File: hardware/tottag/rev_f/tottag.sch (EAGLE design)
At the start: 154 parts, among them J1 MICRO_USB_B_HIROSE_ZX62-B-5PA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, J2 CON_MICRO_SDDM3AT-SF-PEJM5, J3 BAT_HOLE, J4 TC2030-JLINK-NL, J5 TC2030-JLINK-NL, T1 HHM1595A1, U1 DW1000, U10 STM32F091CC, U11 AB1815-T3, U2 FT232RQ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

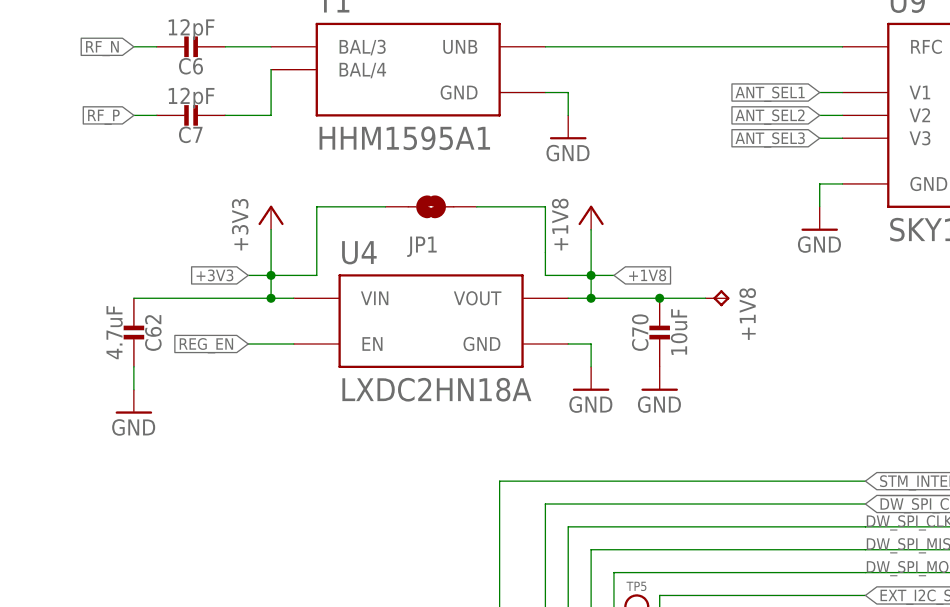
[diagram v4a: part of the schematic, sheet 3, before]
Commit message: Replace obsolete power regulator
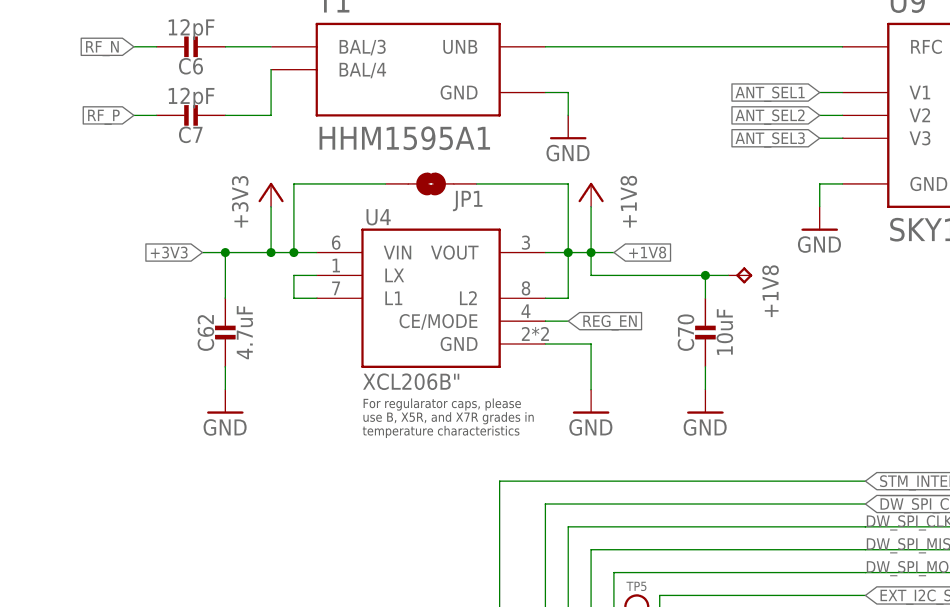
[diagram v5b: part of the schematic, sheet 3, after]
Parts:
- C70: device passives:CAPACITOR0603_CAP -> passives:CAPACITOR0402_CAP
- U4: value LXDC2HN18A -> XCL206B"; device regulators:LXDC2HN18A -> regulators:XCL206B"
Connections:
- new net N$44: U4.L1, U4.LX
- net +1V8: now also U4.L2
- net +3V3: now also C62.1; no longer C62.2
- net GND: now also C62.2; no longer C62.1
- net REG_EN: now also U4.CE/MODE; no longer U4.EN
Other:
- note added: "For regularator caps, please use B, X5R, and X7R grades in temperature characteristics"
- moved on the sheet: +1V8, C62, C70, JP1

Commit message: rev f cleanups
 - Fix footprint error in new regulator
 - Better shielding between 1.8V and debug signals
 - Better routing for `REG_EN` line
 - Clean up ground plane odditites
 - Remove vias from under RTC battery
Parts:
- U4: value XCL206B" -> (none); device regulators:XCL206B" -> regulators:XCL206B
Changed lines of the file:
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@@
 <attribute name="MPN" value="RC0402JR-0710KL"/>
 </part>
-<part name="U4" library="regulators" deviceset="XCL206B" device="&quot;"/>
 <part name="C62" library="passives" deviceset="CAPACITOR" device="0402_CAP" value="4.7uF"/>
 <part name="C70" library="passives" deviceset="CAPACITOR" device="0402_CAP" value="10uF"/>
+<part name="U4" library="regulators" deviceset="XCL206" device="B"/>
 </parts>
 <sheets>
@@
 <attribute name="VALUE" x="43.18" y="162.56" size="1.778" layer="96" font="vector" align="top-left" display="off"/>
 </instance>
-<instance part="U4" gate="G$1" x="45.72" y="152.4" smashed="yes">
-<attribute name="NAME" x="38.354" y="160.528" size="1.778" layer="95"/>
-<attribute name="VALUE" x="38.1" y="142.24" size="1.778" layer="96"/>
-</instance>
 <instance part="C62" gate="G$1" x="22.86" y="149.86" smashed="yes">
 <attribute name="NAME" x="21.59" y="148.59" size="1.778" layer="95" ratio="12" rot="R90" align="bottom-center"/>
@@
 <attribute name="VALUE" x="77.47" y="148.59" size="1.778" layer="96" ratio="12" rot="R270" align="bottom-center"/>
 </instance>
+<instance part="U4" gate="G$1" x="45.72" y="152.4" smashed="yes">
+<attribute name="NAME" x="38.354" y="160.528" size="1.778" layer="95"/>
+<attribute name="VALUE" x="38.1" y="142.24" size="1.778" layer="96"/>
+</instance>
 </instances>
 <busses>
@@
 <wire x1="60.96" y1="157.48" x2="63.5" y2="157.48" width="0.1524" layer="91"/>
 <pinref part="JP1" gate="G$1" pin="2"/>
-<pinref part="U4" gate="G$1" pin="VOUT"/>
 <wire x1="60.96" y1="157.48" x2="58.42" y2="157.48" width="0.1524" layer="91"/>
 <junction x="60.96" y="157.48"/>
 <wire x1="60.96" y1="157.48" x2="60.96" y2="152.4" width="0.1524" layer="91"/>
-<pinref part="U4" gate="G$1" pin="L2"/>
 <wire x1="60.96" y1="152.4" x2="58.42" y2="152.4" width="0.1524" layer="91"/>
 <pinref part="C70" gate="G$1" pin="1"/>
 <wire x1="76.2" y1="152.4" x2="76.2" y2="154.94" width="0.1524" layer="91"/>
 <junction x="76.2" y="154.94"/>
+<pinref part="U4" gate="G$1" pin="L2"/>
+<pinref part="U4" gate="G$1" pin="VOUT"/>
 </segment>
 <segment>
@@
 <wire x1="30.48" y1="165.1" x2="40.64" y2="165.1" width="0.1524" layer="91"/>
 <pinref part="JP1" gate="G$1" pin="1"/>
-<pinref part="U4" gate="G$1" pin="VIN"/>
 <wire x1="30.48" y1="157.48" x2="33.02" y2="157.48" width="0.1524" layer="91"/>
 <junction x="30.48" y="157.48"/>
@@
 <wire x1="22.86" y1="152.4" x2="22.86" y2="157.48" width="0.1524" layer="91"/>
 <junction x="22.86" y="157.48"/>
+<pinref part="U4" gate="G$1" pin="VIN"/>
 </segment>
 <segment>
@@
 <net name="N$44" class="0">
 <segment>
-<pinref part="U4" gate="G$1" pin="LX"/>
 <wire x1="33.02" y1="154.94" x2="30.48" y2="154.94" width="0.1524" layer="91"/>
 <wire x1="30.48" y1="154.94" x2="30.48" y2="152.4" width="0.1524" layer="91"/>
-<pinref part="U4" gate="G$1" pin="L1"/>
 <wire x1="30.48" y1="152.4" x2="33.02" y2="152.4" width="0.1524" layer="91"/>
+<pinref part="U4" gate="G$1" pin="LX"/>
+<pinref part="U4" gate="G$1" pin="L1"/>
 </segment>
 </net>

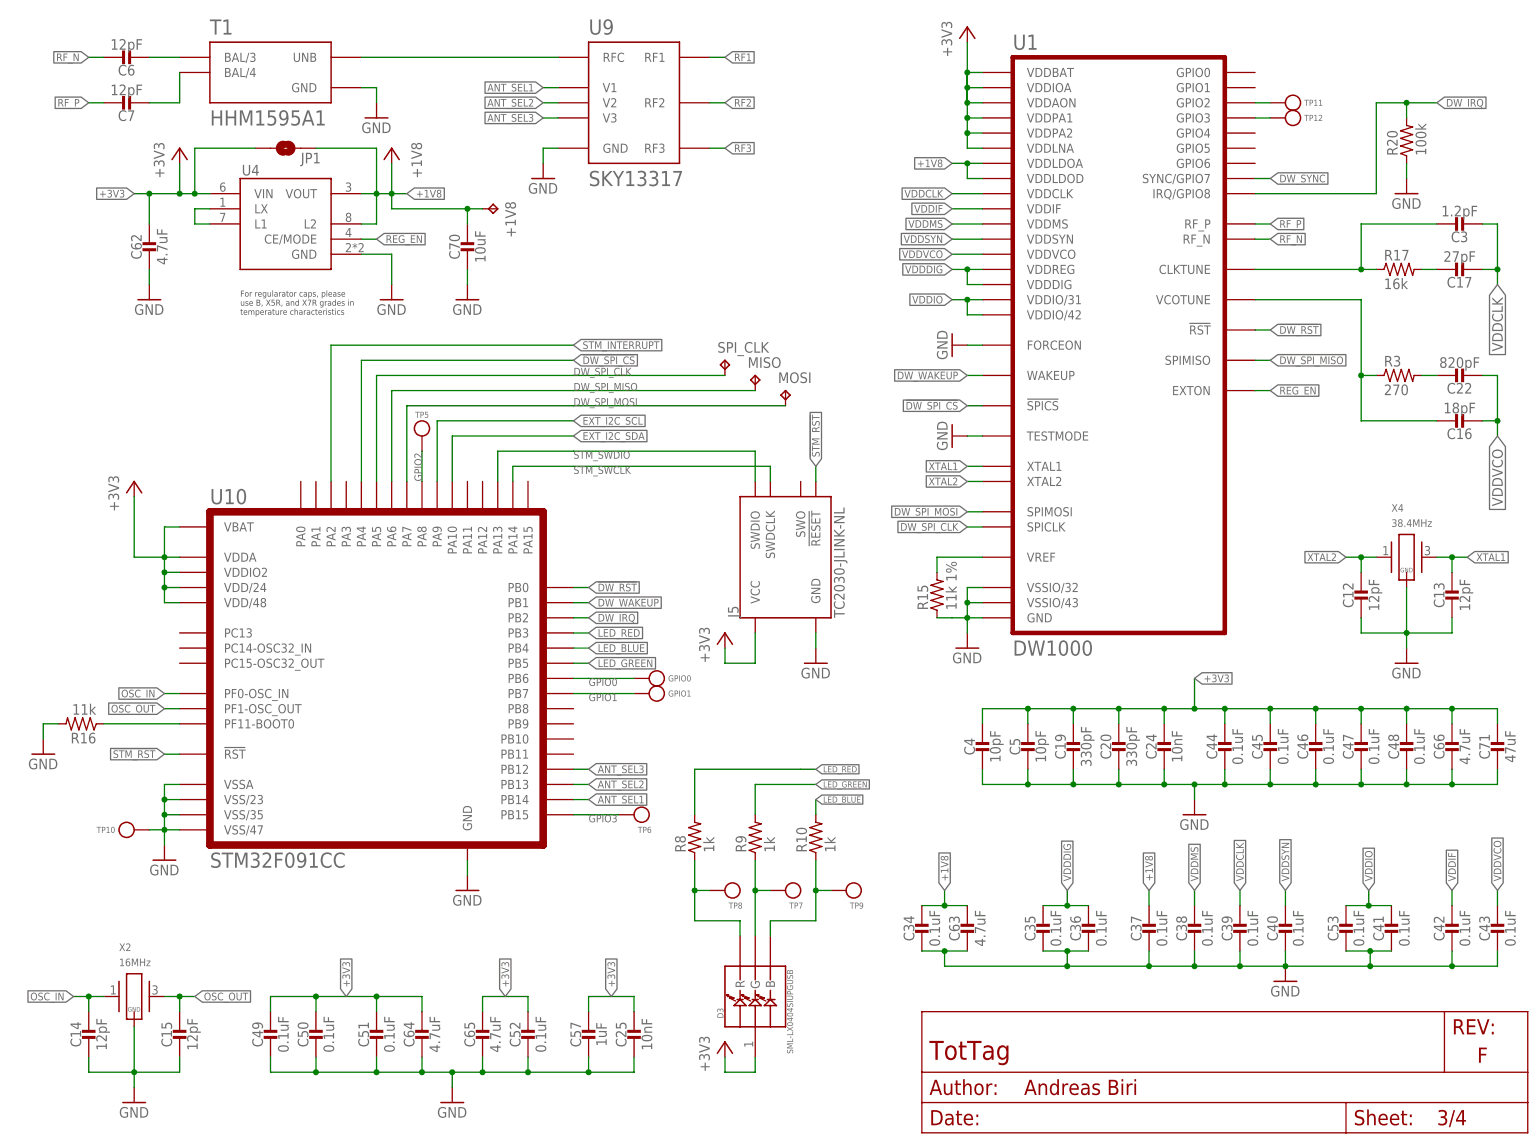
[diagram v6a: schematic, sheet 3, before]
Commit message: fix capacitor, resistor numbering
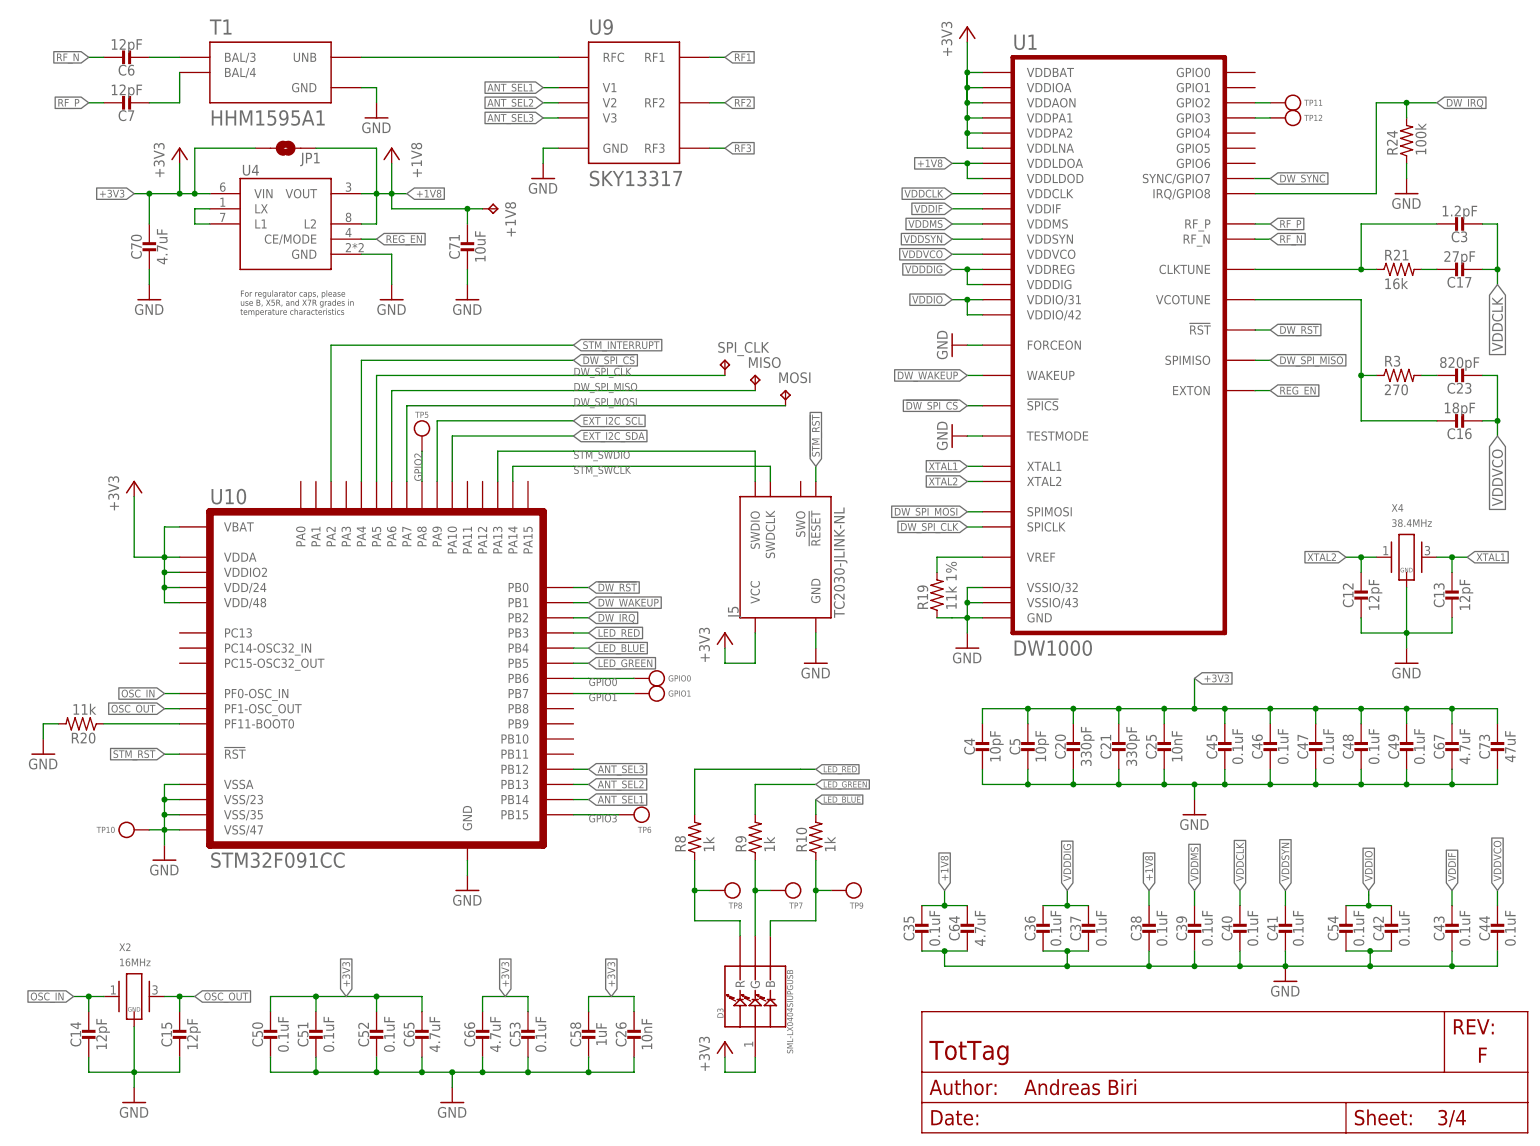
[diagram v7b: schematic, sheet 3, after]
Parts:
- C18: value 100pF -> 47pF; DIGIKEY 490-5922-1-ND -> 490-5942-1-ND; MPN GRM1555C1H101JA01D -> GRM1555C1H470JA01D
- C19: value 330pF -> 100pF; DIGIKEY (none) -> 490-5922-1-ND; MPN (none) -> GRM1555C1H101JA01D
- C21: value 820pF -> 330pF; DIGIKEY 1276-6989-1-ND -> (none); MPN CL05C821JB5NFNC -> (none)
- C22: DIGIKEY (none) -> 1276-6989-1-ND; MPN (none) -> CL05C821JB5NFNC
- C23: value 10nF -> 820pF
- C26: value 47nF -> 10nF; DIGIKEY 445-1264-1-ND -> (none); MPN C1005X7R1C473K050BC -> (none)
- C27: value 0.1uF -> 47nF; DIGIKEY (none) -> 445-1264-1-ND; MPN (none) -> C1005X7R1C473K050BC
- C28: DIGIKEY 490-6328-1-ND -> (none); MPN GRM155R71C104KA88J -> (none)
- C31: DIGIKEY (none) -> 490-6328-1-ND; MPN (none) -> GRM155R71C104KA88J
- C54: value 1uF -> 0.1uF
- C56: DIGIKEY 490-7195-1-ND -> (none); MPN GRM155R70G105KA12D -> (none)
- C57: DIGIKEY (none) -> 490-7195-1-ND; MPN (none) -> GRM155R70G105KA12D
- C58: value 4.7uF -> 1uF
- C59: value 4.7uF -> 1uF; DIGIKEY (none) -> 490-7195-1-ND; MPN (none) -> GRM155R70G105KA12D
- C60: DESCRIPTION CAP CER 4.7UF 6.3V X5R 0402 -> (none); DIGIKEY 445-5947-1-ND -> (none); MANUFACTURER TDK -> (none); MPN C1005X5R0J475K050BC -> (none)
- C62: DESCRIPTION (none) -> CAP CER 4.7UF 6.3V X5R 0402; DIGIKEY (none) -> 445-5947-1-ND; MANUFACTURER (none) -> TDK; MPN (none) -> C1005X5R0J475K050BC
- C69: value 10uF -> 4.7uF; device passives:CAPACITOR0603_CAP -> passives:CAPACITOR0402_CAP; DIGIKEY 490-3896-1-ND -> (none); MPN GRM188R60J106ME47D -> (none)
- C70: value 10uF -> 4.7uF
- C71: value 47uF -> 10uF; device passives:CAPACITOR0603_CAP -> passives:CAPACITOR0402_CAP
- C72: value 47pF -> 10uF; device passives:CAPACITOR0402_CAP -> passives:CAPACITOR0603_CAP; DIGIKEY 490-5942-1-ND -> 490-3896-1-ND; MPN GRM1555C1H470JA01D -> GRM188R60J106ME47D
- C73: value 1uF -> 47uF; device passives:CAPACITOR0402_CAP -> passives:CAPACITOR0603_CAP; DIGIKEY 490-7195-1-ND -> (none); MPN GRM155R70G105KA12D -> (none)
- R11: value 2k 1% -> 1.41k; DIGIKEY (none) -> 311-10KJRCT-ND; MPN (none) -> RC0402JR-0710KL
- R12: value 10k -> 2k 1%
- R15: value 11k 1% -> 10k
- R16: value 11k -> 10k; DIGIKEY (none) -> 311-10KJRCT-ND; MPN (none) -> RC0402JR-0710KL
- R17: value 16k -> 10k; DIGIKEY (none) -> 311-10KJRCT-ND; MPN (none) -> RC0402JR-0710KL
- R18: value 100k -> 10k; DIGIKEY (none) -> 311-10KJRCT-ND; MPN (none) -> RC0402JR-0710KL
- R19: value 100k -> 11k 1%
- R20: value 100k -> 11k
- R21: value 2.2M -> 16k
- R22: value 10M -> 100k
- R23: value 10k -> 100k; DIGIKEY 311-10KJRCT-ND -> (none); MPN RC0402JR-0710KL -> (none)
- R24: value 1.41k -> 100k; DIGIKEY 311-10KJRCT-ND -> (none); MPN RC0402JR-0710KL -> (none)
- R25: value 10k -> 2.2M; DIGIKEY 311-10KJRCT-ND -> (none); MPN RC0402JR-0710KL -> (none)
- R26: value 10k -> 10M; DIGIKEY 311-10KJRCT-ND -> (none); MPN RC0402JR-0710KL -> (none)
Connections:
- net !NRF_CS_RTC: now also R18.1; no longer R26.1
- net !NRF_CS_SD: now also R14.1; no longer R13.1
- net !SD_DETECT: now also R23.1; no longer R19.1
- net +1V8: now also C35.1, C38.1, C64.1, C71.1; no longer C34.1, C37.1, C63.1, C70.1
- net +3V3: now also C21.1, C26.1, C34.1, C53.1, C56.1, C58.1, C63.1, C67.1, C70.1, C72.1, C73.1; no longer C19.1, C24.1, C29.1, C44.1, C55.1, C57.1, C59.1, C62.1, C64.1, C69.1, C71.1
- net BATIN: now also C28.2, R25.2, R26.1; no longer C27.2, R21.2, R22.1
- net DW_IRQ: now also R24.2; no longer R20.2
- net GND: now also C22.2, C27.2, C28.1, R12.1, R19.1, R20.2, R22.2, R24.1, R25.1; no longer C23.2, C27.1, C28.2, R11.1, R15.1, R16.2, R18.2, R20.1, R21.1
- net N$1: now also C29.1; no longer C28.1
- net N$10: now also C19.1; no longer C18.1
- net N$11: now also C24.1; no longer C23.1
- net N$12: now also R21.2; no longer R17.2
- net N$13: now also R12.2; no longer R11.2
- net N$16: now also R21.1; no longer R17.1
- net N$2: now also C22.1; no longer C21.1
- net N$21: now also R19.2; no longer R15.2
- net N$22: now also R20.1; no longer R16.1
- net N$35: now also C18.1; no longer C72.1
- net N$43: now also R16.1; no longer R23.1
- net N$45: now also R11.2; no longer R24.2
- net N$55: now also C62.1, R15.2, R23.2; no longer C60.1, R12.2, R19.2
- net N$8: now also C23.1; no longer C22.1
- net N$9: now also C27.1, C57.1; no longer C26.1, C56.1
- net NRF_MISO: now also R15.1; no longer R14.1
- net NRF_MOSI: now also R13.1; no longer R12.1
- net RTC_WDI: now also R17.1; no longer R25.1
- net SD_EN: now also R22.1; no longer R18.1
- net VBAT: now also C60.1, C69.1, R26.2; no longer C58.1, C68.1, R22.2
- net VBAT_RTC: now also R11.1, R16.2, R17.2, R18.2; no longer R23.2, R24.1, R25.2, R26.2
- net VCC: now also C59.1; no longer C73.1
- net VDDCLK: now also C40.1; no longer C39.1
- net VDDDIG: now also C37.1; no longer C35.1
- net VDDIF: now also C43.1; no longer C42.1
- net VDDIO: now also C42.1, C54.1; no longer C41.1, C53.1
- net VDDMS: now also C39.1; no longer C38.1
- net VDDSYN: now also C41.1; no longer C40.1
- net VDDVCO: now also C23.2, C44.1; no longer C22.2, C43.1
- net VUSB: now also C55.1, C68.1; no longer C54.1, C67.1
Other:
- moved on the sheet: C18, C20, C25, C28, C29, C31, C35, C36, C37, C38, C39, C40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
